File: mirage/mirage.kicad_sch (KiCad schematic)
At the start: 1 part, among them U1 STM32U575VGT6

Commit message: feat: initialize structure
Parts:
- removed U1: STM32U575VGT6, EasyEDA:LQFP-100_L14.0-W14.0-P0.50-LS16.0-BL, symbol EasyEDA:STM32U575VGT6
- added C1, C2, C3, C4: 100nF, symbol Device:C
- added FB1: FerriteBead, symbol Device:FerriteBead
- added U1: STM32U575VGT6, Package_QFP:LQFP-100_14x14mm_P0.5mm, symbol MCU_ST_STM32U5:STM32U575VGTx
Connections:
- new net +3.3V: C1.1, C2.1, C3.1, C4.1, U1.100 (VDD), U1.11 (VDD), U1.28 (VDD), U1.50 (VDD), U1.75 (VDD)
- new net GND: C1.2, C2.2, C3.2, C4.2, U1.10 (VSS), U1.19 (VSSA), U1.27 (VSS), U1.49 (VSS), U1.74 (VSS), U1.99 (VSS)
- new net YELLOW_LED: U1.72 (PA13)

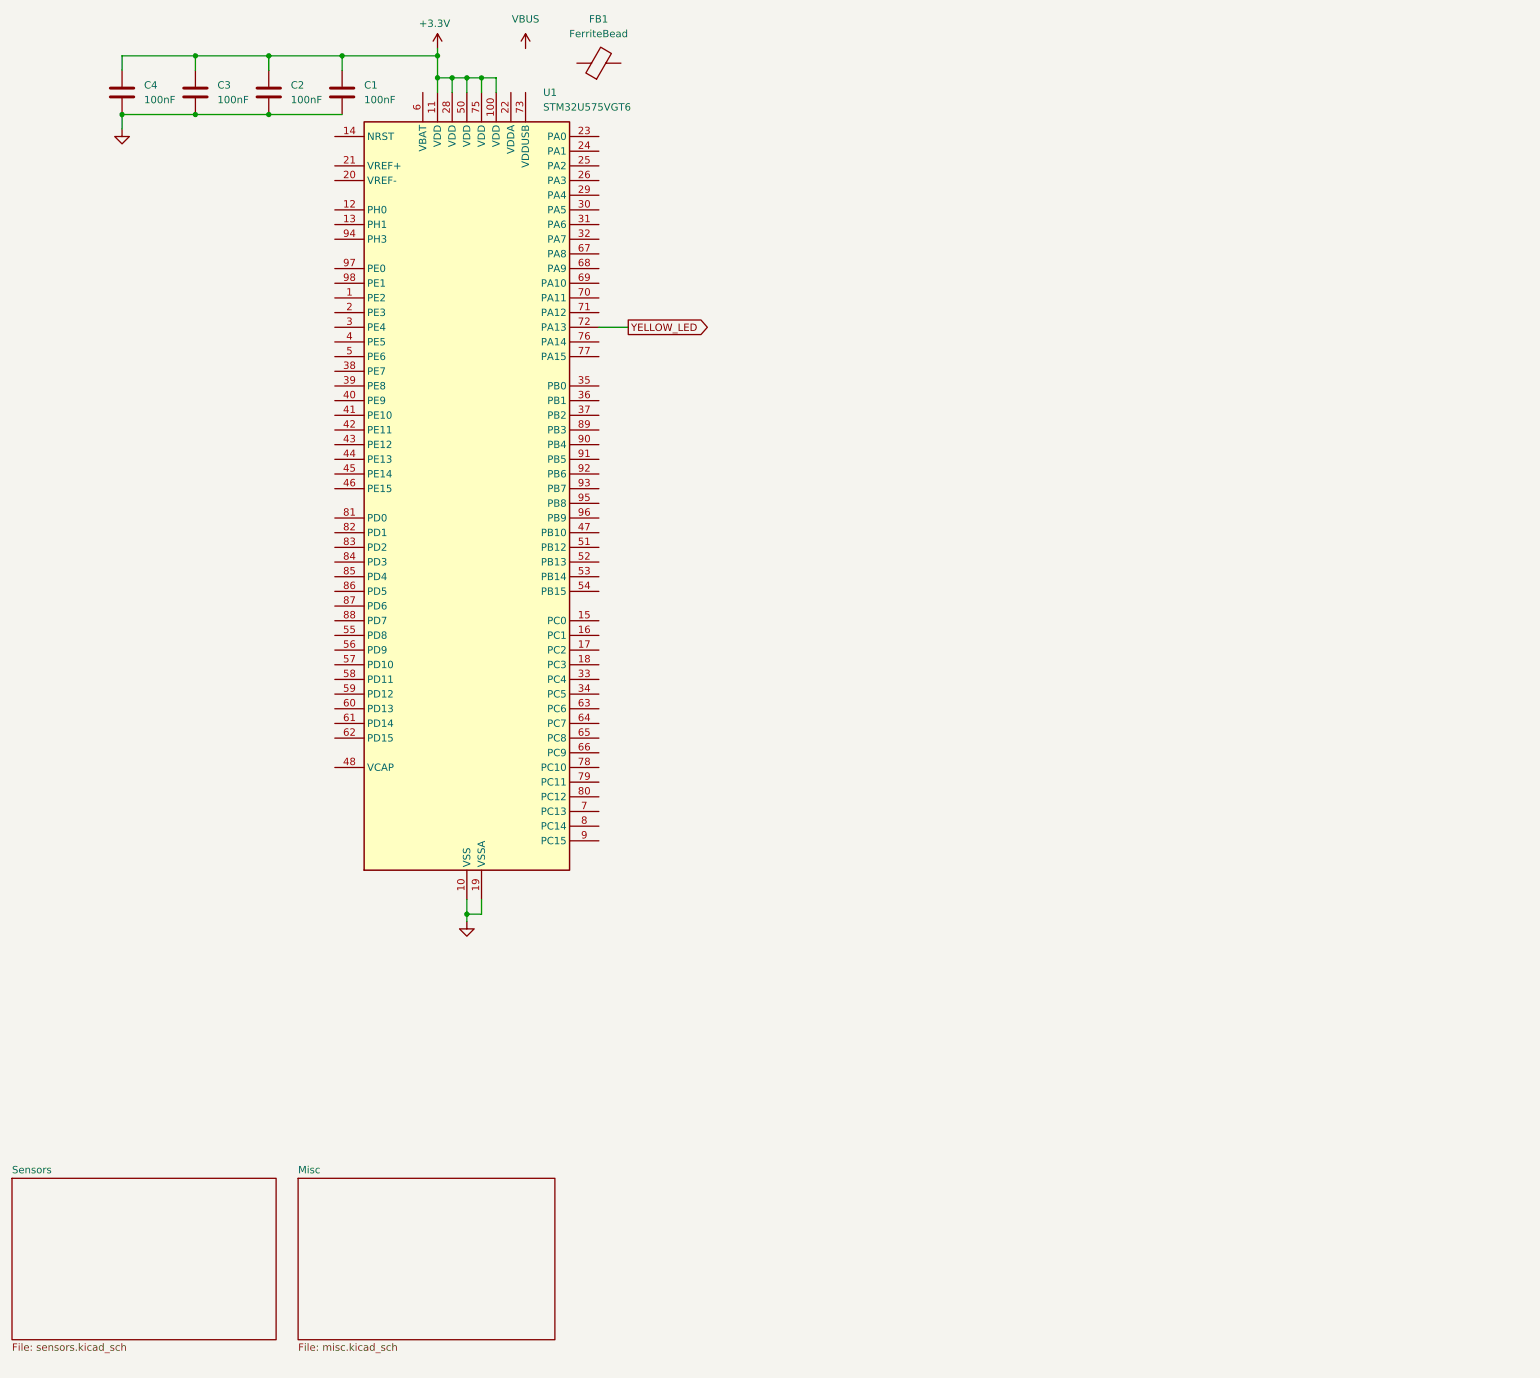
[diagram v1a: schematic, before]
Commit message: feat(sensor): fundamental sensor lists
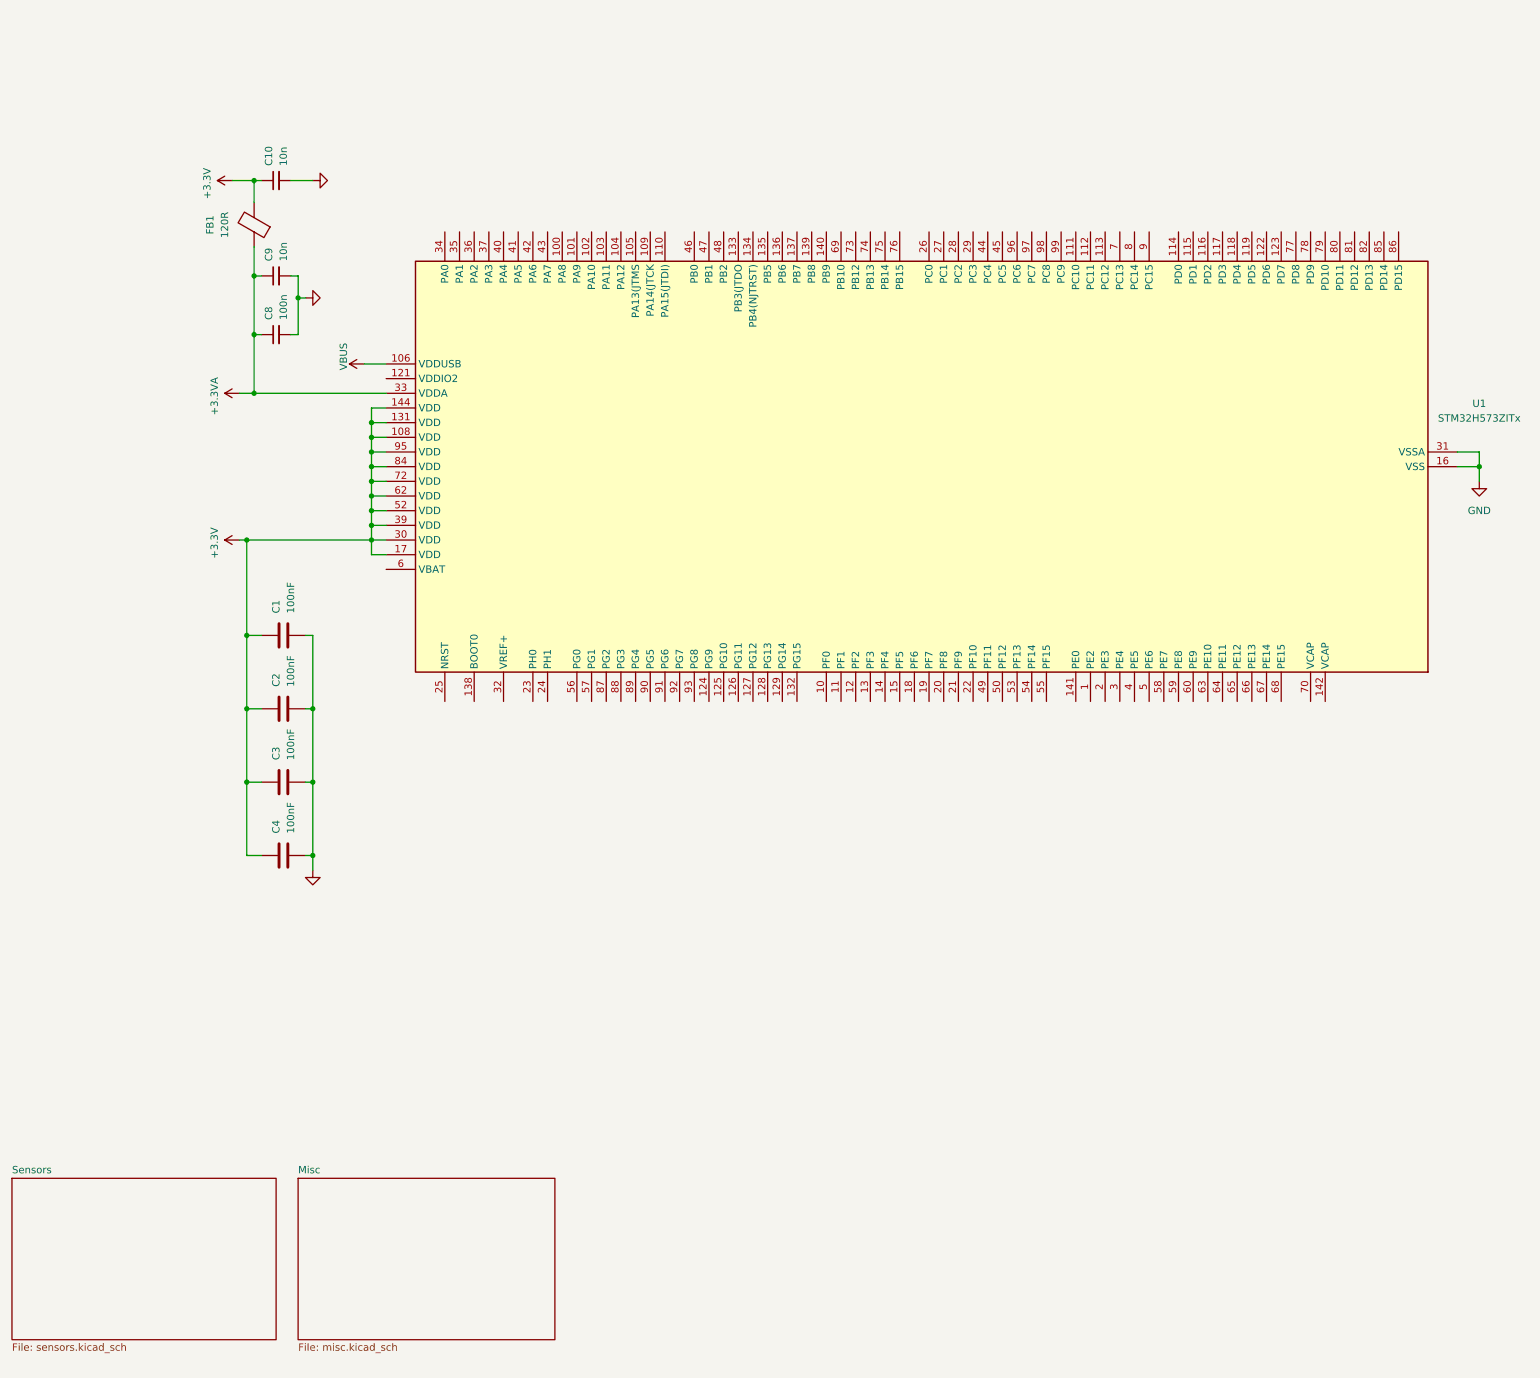
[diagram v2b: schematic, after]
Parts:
- removed U1: STM32U575VGT6, Package_QFP:LQFP-100_14x14mm_P0.5mm, symbol MCU_ST_STM32U5:STM32U575VGTx
- added C10, C9: 10n, Capacitor_SMD:C_0402_1005Metric, symbol Device:C_Small
- added C8: 100n, Capacitor_SMD:C_0402_1005Metric, symbol Device:C_Small
- added U1: STM32H573ZITx, Package_QFP:LQFP-144_20x20mm_P0.5mm, symbol MCU_ST_STM32H5:STM32H573ZITx
- C1, C2, C3, C4: footprint (none) -> Capacitor_SMD:C_0402_1005Metric
- FB1: value FerriteBead -> 120R; footprint (none) -> Inductor_SMD:L_0603_1608Metric
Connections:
- net +3.3V: now also FB1.2, C10.1, U1.108 (VDD), U1.131 (VDD), U1.144 (VDD), U1.17 (VDD), U1.30 (VDD), U1.39 (VDD), U1.52 (VDD), U1.62 (VDD), U1.72 (VDD), U1.84 (VDD), U1.95 (VDD)
- net GND: now also C10.2, C8.2, C9.2, U1.107 (VSS), U1.120 (VSS), U1.130 (VSS), U1.143 (VSS), U1.16 (VSS), U1.31 (VSSA), U1.38 (VSS), U1.51 (VSS), U1.61 (VSS), U1.71 (VSS), U1.83 (VSS), U1.94 (VSS)
- net VBUS: now also U1.106 (VDDUSB)
- net +3.3VA: now reaches FB1.1
- net +3.3VA: now also C8.1, C9.1, U1.33 (VDDA)
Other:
- moved on the sheet: C1, C2, C3, C4, FB1

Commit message: feat: connectors
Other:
- added sheet Connectors (connectors.kicad_sch)
- added sheet Power (power.kicad_sch)

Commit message: lolo
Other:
- added sheet abcd (abcd.kicad_sch)
